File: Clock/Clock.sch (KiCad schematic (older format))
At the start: 50 parts, among them J1 Reset Mode, J2 Clock Select, J3 I/O, SW1 Pulse, SW2 Mode, U1 74HC74, U2 74HC14, U3 LMC555CN, U4 74HC74, U5 CD4053, U6 DS1813

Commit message: Update clock
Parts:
- C1, C2, C3, C5, C6, C7, C8: footprint (none) -> Capacitor_THT:CP_Radial_D4.0mm_P2.00mm
- C10, C11, C12, C13, C9: footprint (none) -> Capacitor_THT:C_Disc_D5.0mm_W2.5mm_P2.50mm
- C4: footprint (none) -> Capacitor_THT:C_Disc_D6.0mm_W2.5mm_P5.00mm
- D1, D2, D3, D4, D5: footprint (none) -> LED_THT:LED_D3.0mm
- H1, H2, H3, H4: footprint (none) -> MountingHole:MountingHole_3.2mm_M3_Pad
- J1, J2: footprint (none) -> Connector_PinSocket_2.54mm:PinSocket_1x03_P2.54mm_Vertical
- J3: footprint (none) -> Connector_PinSocket_2.54mm:PinSocket_1x07_P2.54mm_Vertical
- R1, R10, R11, R12, R13, R14, R15, R16, R2, R3, R4, R5, R6, R7, R8, R9: footprint (none) -> Resistor_THT:R_Axial_DIN0207_L6.3mm_D2.5mm_P7.62mm_Horizontal
- RV1: footprint (none) -> Potentiometer_THT:Potentiometer_Piher_PC-16_Single_Horizontal
- SW1, SW2: footprint (none) -> Button_Switch_THT:SW_PUSH_6mm
- U1, U2, U4: footprint (none) -> Package_DIP:DIP-14_W7.62mm
- U3: footprint (none) -> Package_DIP:DIP-8_W7.62mm
- U5: footprint (none) -> Package_DIP:DIP-16_W7.62mm
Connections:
- net at R7.2, U3.7 (DIS): now also RV1.1; no longer RV1.2
- net at R6.2: now also RV1.2; no longer RV1.3
- no-connect marks 4 -> 6
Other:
- moved on the sheet: R6, RV1

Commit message: Update clock
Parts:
- C8: value 1uF -> 10uF
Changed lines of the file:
@@
 P 8400 6050
 F 0 "C8" H 8518 6096 50  0000 L CNN
-F 1 "1uF" H 8518 6005 50  0000 L CNN
+F 1 "10uF" H 8518 6005 50  0000 L CNN
 F 2 "Capacitor_THT:CP_Radial_D4.0mm_P2.00mm" H 8438 5900 50  0001 C CNN
 F 3 "~" H 8400 6050 50  0001 C CNN

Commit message: Fixed clock
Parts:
- R7: value 10K -> 1K
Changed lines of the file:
@@
 P 3750 1200
 F 0 "R7" H 3820 1246 50  0000 L CNN
-F 1 "10K" H 3820 1155 50  0000 L CNN
+F 1 "1K" H 3820 1155 50  0000 L CNN
 F 2 "Resistor_THT:R_Axial_DIN0207_L6.3mm_D2.5mm_P7.62mm_Horizontal" V 3680 1200 50  0001 C CNN
 F 3 "~" H 3750 1200 50  0001 C CNN

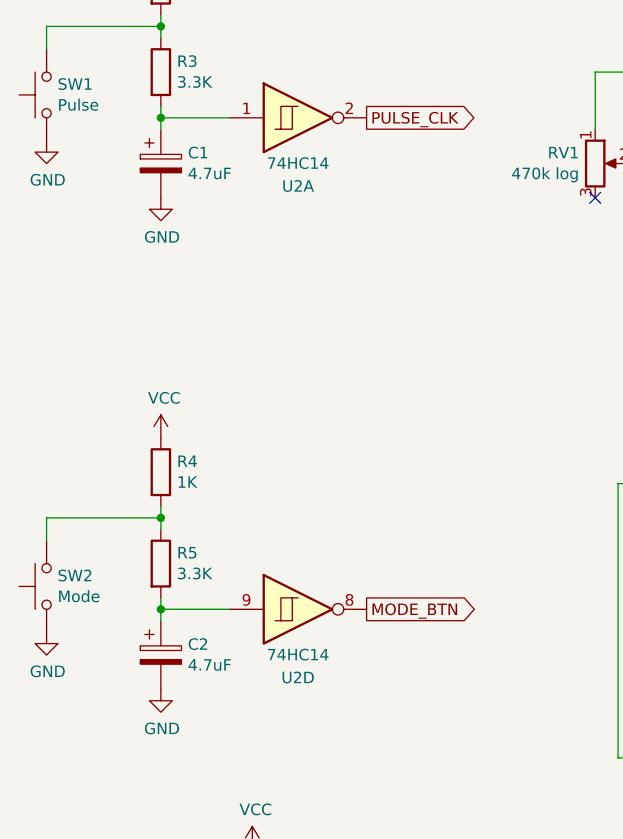
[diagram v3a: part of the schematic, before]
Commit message: Fix component values
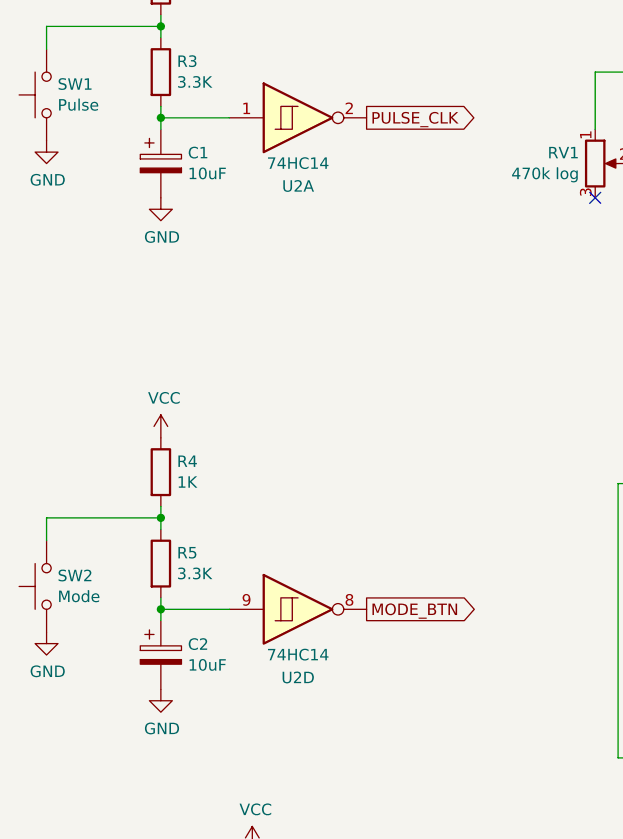
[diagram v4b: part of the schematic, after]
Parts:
- C1, C2: value 4.7uF -> 10uF
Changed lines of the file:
@@
 P 1350 1900
 F 0 "C1" H 1468 1946 50  0000 L CNN
-F 1 "4.7uF" H 1468 1855 50  0000 L CNN
+F 1 "10uF" H 1468 1855 50  0000 L CNN
 F 2 "Capacitor_THT:CP_Radial_D4.0mm_P2.00mm" H 1388 1750 50  0001 C CNN
 F 3 "~" H 1350 1900 50  0001 C CNN
@@
 P 1350 4050
 F 0 "C2" H 1468 4096 50  0000 L CNN
-F 1 "4.7uF" H 1468 4005 50  0000 L CNN
+F 1 "10uF" H 1468 4005 50  0000 L CNN
 F 2 "Capacitor_THT:CP_Radial_D4.0mm_P2.00mm" H 1388 3900 50  0001 C CNN
 F 3 "~" H 1350 4050 50  0001 C CNN
